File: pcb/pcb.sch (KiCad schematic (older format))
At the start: 19 parts, among them J1 USB_C_Receptacle_USB2.0, SW1 SW_Push, U1 ATmega32U4-AU, U2 PRTR5V0U2X, Y1 16MHz

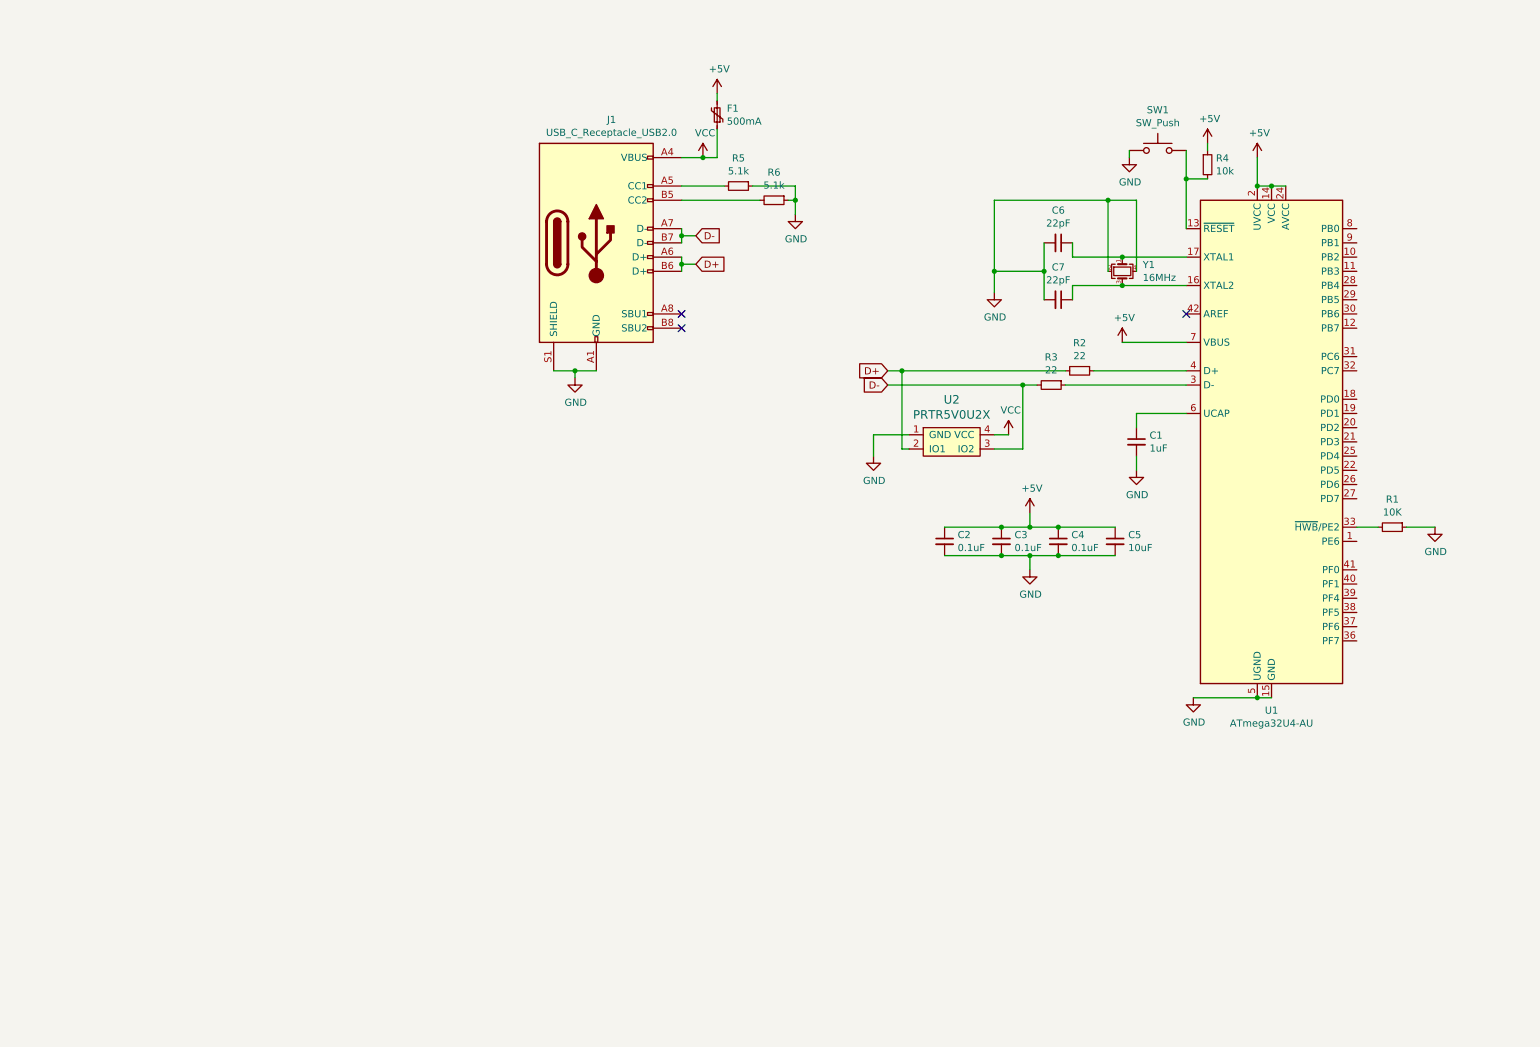
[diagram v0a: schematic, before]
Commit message: set up switch matrix
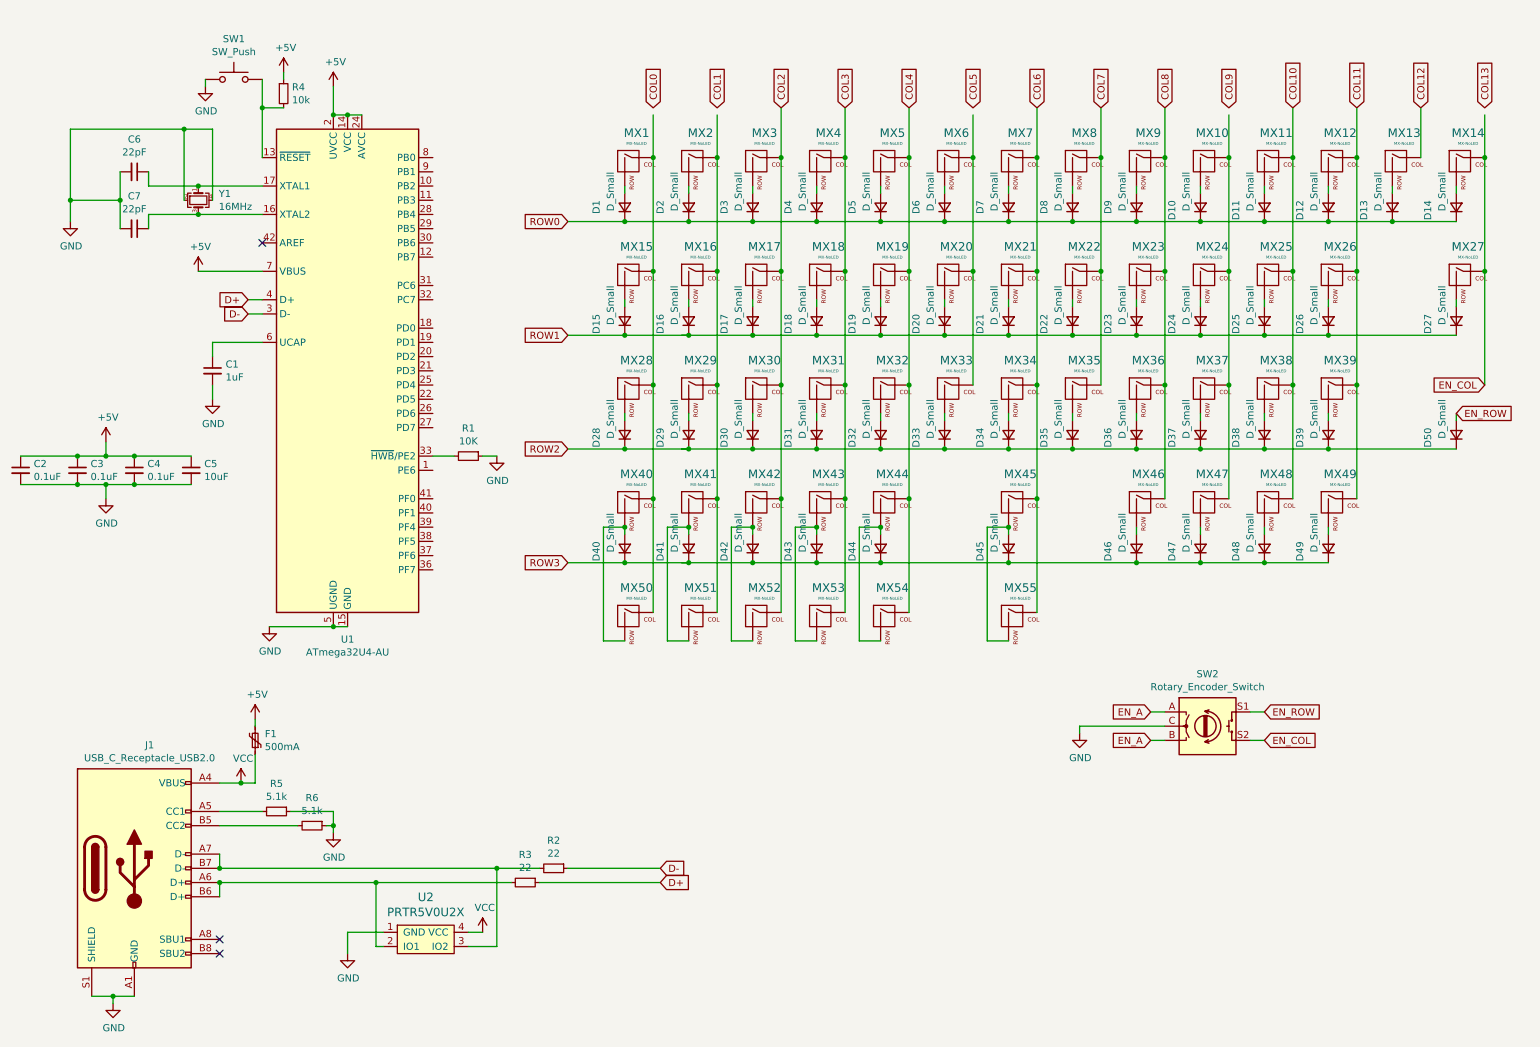
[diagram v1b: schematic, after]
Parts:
- added D1, D10, D11, D12, D13, D14, D15, D16, D17, D18, D19, D2, D20, D21, D22, D23, D24, D25, D26, D27, D28, D29, D3, D30, D31, D32, D33, D34, D35, D36, D37, D38, D39, D4, D40, D41, D42, D43, D44, D45, D46, D47, D48, D49, D5, D50, D6, D7, D8, D9: D_Small, symbol Device:D_Small
- added MX1, MX10, MX11, MX12, MX13, MX14, MX15, MX16, MX17, MX18, MX19, MX2, MX20, MX21, MX22, MX23, MX24, MX25, MX26, MX27, MX28, MX29, MX3, MX30, MX31, MX32, MX33, MX34, MX35, MX36, MX37, MX38, MX39, MX4, MX40, MX41, MX42, MX43, MX44, MX45, MX46, MX47, MX48, MX49, MX5, MX50, MX51, MX52, MX53, MX54, MX55, MX6, MX7, MX8, MX9: MX-NoLED, symbol MX_Alps_Hybrid:MX-NoLED
- added SW2: Rotary_Encoder_Switch, symbol Device:Rotary_Encoder_Switch
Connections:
- net labels added: COL0, COL1, COL10, COL11, COL12, COL13, COL2, COL3, COL4, COL5, COL6, COL7, COL8, COL9, EN_A, EN_COL, EN_ROW, ROW0, ROW1, ROW2, ROW3
- wire segments 73 -> 254
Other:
- moved on the sheet: C1, C2, C3, C4, C5, C6, C7, F1, J1, R1, R2, R3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

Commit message: assign footprints
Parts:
- removed U2: PRTR5V0U2X, symbol random-keyboard-parts:PRTR5V0U2X
- added J2: AVR-ISP-6, symbol Connector:AVR-ISP-6
- added MX56: MX-NoLED, MX_Alps_Hybrid:MX-2U, symbol MX_Alps_Hybrid:MX-NoLED
- C1, C2, C3, C4, C5, C6, C7: footprint (none) -> Capacitor_SMD:C_0805_2012Metric
- D1, D10, D11, D12, D13, D14, D15, D16, D17, D18, D19, D2, D20, D21, D22, D23, D24, D25, D26, D27, D28, D29, D3, D30, D31, D32, D33, D34, D35, D36, D37, D38, D39, D4, D40, D41, D42, D43, D44, D45, D46, D47, D48, D49, D5, D50, D6, D7, D8, D9: footprint (none) -> Diode_SMD:D_SOD-123
- E1: renamed from SW2; footprint (none) -> Rotary_Encoder:RotaryEncoder_Alps_EC11E_Vertical_H20mm
- F1: footprint (none) -> Fuse:Fuse_1206_3216Metric
- J1: footprint (none) -> Connector_USB:USB_C_Receptacle_Palconn_UTC16-G
- MX1, MX10, MX11, MX12, MX13, MX14, MX16, MX17, MX18, MX19, MX2, MX20, MX21, MX22, MX23, MX24, MX25, MX27, MX29, MX3, MX30, MX31, MX32, MX33, MX34, MX35, MX36, MX37, MX38, MX4, MX40, MX41, MX42, MX43, MX46, MX47, MX48, MX49, MX5, MX6, MX7, MX8, MX9: footprint (none) -> MX_Alps_Hybrid:MX-1U
- MX15, MX26: footprint (none) -> MX_Alps_Hybrid:MX-1.5U
- MX28: footprint (none) -> MX_Alps_Hybrid:MX-1.75U
- MX39, MX50, MX51, MX52, MX53, MX55: footprint (none) -> MX_Alps_Hybrid:MX-1.25U
- MX44, MX54: footprint (none) -> MX_Alps_Hybrid:MX-2.75U
- MX45: footprint (none) -> MX_Alps_Hybrid:MX-2.25U
- R1, R2, R3, R4, R5, R6: footprint (none) -> Resistor_SMD:R_0805_2012Metric
- SW1: footprint (none) -> Button_Switch_SMD:SW_SPST_EVQP7C
- Y1: footprint (none) -> Crystal:Crystal_SMD_3225-4Pin_3.2x2.5mm
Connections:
- net labels added: E_A, E_B, E_COL, E_ROW, MISO, MOSI, RST, SCK
- net labels removed: EN_A, EN_COL, EN_ROW
- wire segments 254 -> 257
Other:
- moved on the sheet: D1, D10, D11, D12, D13, D14, D15, D16, D17, D18, D19, D2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

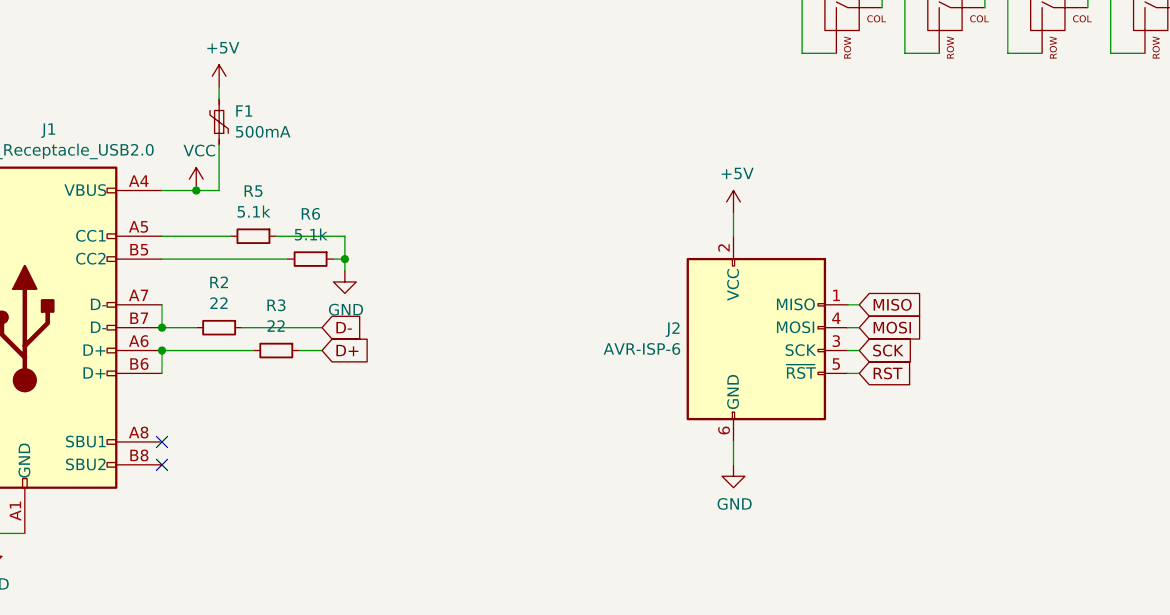
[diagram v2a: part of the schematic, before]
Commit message: add isp footprints
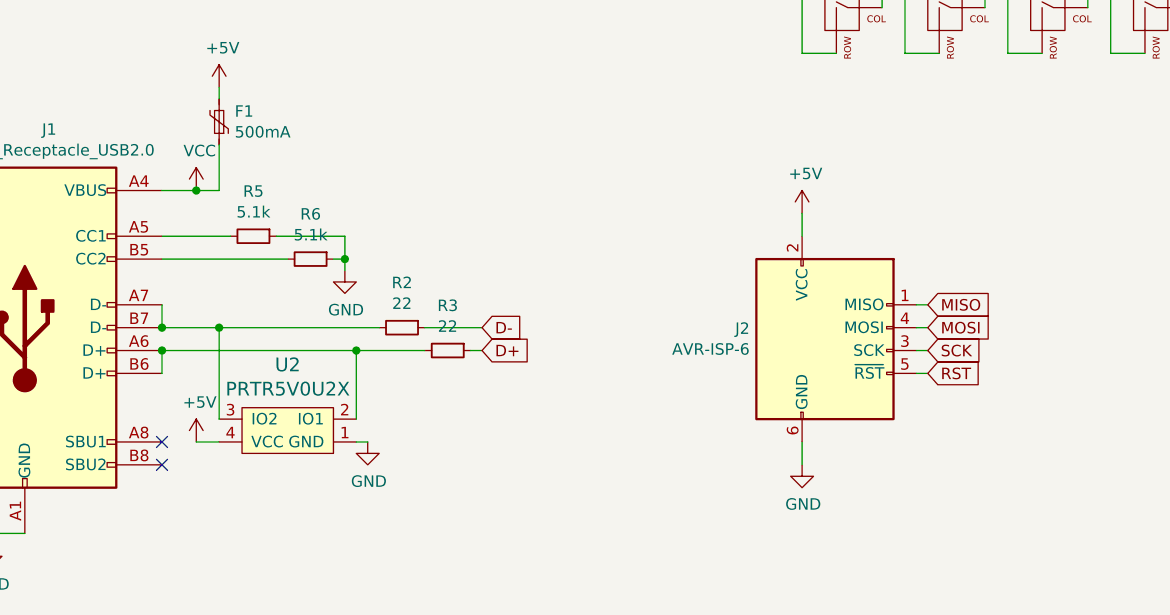
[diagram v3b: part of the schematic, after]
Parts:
- added U2: PRTR5V0U2X, random-keyboard-parts:SOT143B, symbol random-keyboard-parts:PRTR5V0U2X
- J2: footprint (none) -> random-keyboard-parts:Reset_Pretty
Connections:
- wire segments 257 -> 263
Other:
- moved on the sheet: J2, R2, R3
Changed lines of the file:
@@
 Wire Wire Line
 	2050 6400 2050 6500
-Text GLabel 2750 6600 2    50   Input ~ 0
-D+
 $Comp
 L Device:R_Small R2
 U 1 1 61ACD13B
-P 2300 6500
-F 0 "R2" V 2104 6500 50  0000 C CNN
-F 1 "22" V 2195 6500 50  0000 C CNN
-F 2 "Resistor_SMD:R_0805_2012Metric" H 2300 6500 50  0001 C CNN
-F 3 "~" H 2300 6500 50  0001 C CNN
-	1    2300 6500
+P 3100 6500
+F 0 "R2" V 2904 6500 50  0000 C CNN
+F 1 "22" V 2995 6500 50  0000 C CNN
+F 2 "Resistor_SMD:R_0805_2012Metric" H 3100 6500 50  0001 C CNN
+F 3 "~" H 3100 6500 50  0001 C CNN
+	1    3100 6500
 	0    1    1    0
 $EndComp
@@
 L Device:R_Small R3
 U 1 1 61ACDED4
-P 2550 6600
-F 0 "R3" V 2354 6600 50  0000 C CNN
-F 1 "22" V 2445 6600 50  0000 C CNN
-F 2 "Resistor_SMD:R_0805_2012Metric" H 2550 6600 50  0001 C CNN
-F 3 "~" H 2550 6600 50  0001 C CNN
-	1    2550 6600
+P 3300 6600
+F 0 "R3" V 3104 6600 50  0000 C CNN
+F 1 "22" V 3195 6600 50  0000 C CNN
+F 2 "Resistor_SMD:R_0805_2012Metric" H 3300 6600 50  0001 C CNN
+F 3 "~" H 3300 6600 50  0001 C CNN
+	1    3300 6600
 	0    1    1    0
 $EndComp
-Text GLabel 2750 6500 2    50   Input ~ 0
-D-
 Wire Wire Line
 	2300 5450 2300 5500
@@
 	10150 1050 10150 1350
 Connection ~ 10150 1350
-Wire Wire Line
-	2200 6500 2050 6500
 Connection ~ 2050 6500
-Wire Wire Line
-	2050 6600 2450 6600
 Connection ~ 2050 6600
 $Comp
 L power:+5V #PWR0111
 U 1 1 61D89112
-P 4550 6000
-F 0 "#PWR0111" H 4550 5850 50  0001 C CNN
-F 1 "+5V" H 4565 6173 50  0000 C CNN
-F 2 "" H 4550 6000 50  0001 C CNN
-F 3 "" H 4550 6000 50  0001 C CNN
-	1    4550 6000
-	1    0    0    -1
-$EndComp
-Wire Wire Line
-	4550 6000 4550 6100
+P 4850 6000
+F 0 "#PWR0111" H 4850 5850 50  0001 C CNN
+F 1 "+5V" H 4865 6173 50  0000 C CNN
+F 2 "" H 4850 6000 50  0001 C CNN
+F 3 "" H 4850 6000 50  0001 C CNN
+	1    4850 6000
+	1    0    0    -1
+$EndComp
+Wire Wire Line
+	4850 6000 4850 6100
 $Comp
 L power:GND #PWR0112
 U 1 1 61D9AA06
-P 4550 7100
-F 0 "#PWR0112" H 4550 6850 50  0001 C CNN
-F 1 "GND" H 4555 6927 50  0000 C CNN
-F 2 "" H 4550 7100 50  0001 C CNN
-F 3 "" H 4550 7100 50  0001 C CNN
-	1    4550 7100
-	1    0    0    -1
-$EndComp
-Wire Wire Line
-	4550 7000 4550 7100
-Text GLabel 5100 6400 2    50   Input ~ 0
+P 4850 7100
+F 0 "#PWR0112" H 4850 6850 50  0001 C CNN
+F 1 "GND" H 4855 6927 50  0000 C CNN
+F 2 "" H 4850 7100 50  0001 C CNN
+F 3 "" H 4850 7100 50  0001 C CNN
+	1    4850 7100
+	1    0    0    -1
+$EndComp
+Wire Wire Line
+	4850 7000 4850 7100
+Text GLabel 5400 6400 2    50   Input ~ 0
 MISO
-Text GLabel 5100 6500 2    50   Input ~ 0
+Text GLabel 5400 6500 2    50   Input ~ 0
 MOSI
-Text GLabel 5100 6600 2    50   Input ~ 0
+Text GLabel 5400 6600 2    50   Input ~ 0
 SCK
-Text GLabel 5100 6700 2    50   Input ~ 0
+Text GLabel 5400 6700 2    50   Input ~ 0
 RST
 Wire Wire Line
-	5100 6400 5050 6400
-Wire Wire Line
-	5050 6500 5100 6500
+	5400 6400 5350 6400
+Wire Wire Line
+	5350 6500 5400 6500
 $Comp
 L Connector:AVR-ISP-6 J2
 U 1 1 61D861F9
-P 4650 6600
-F 0 "J2" H 4321 6696 50  0000 R CNN
-F 1 "AVR-ISP-6" H 4321 6605 50  0000 R CNN
-F 2 "" V 4400 6650 50  0001 C CNN
-F 3 " ~" H 3375 6050 50  0001 C CNN
-	1    4650 6600
-	1    0    0    -1
-$EndComp
-Wire Wire Line
-	5050 6600 5100 6600
-Wire Wire Line
-	5050 6700 5100 6700
+P 4950 6600
+F 0 "J2" H 4621 6696 50  0000 R CNN
+F 1 "AVR-ISP-6" H 4621 6605 50  0000 R CNN
+F 2 "random-keyboard-parts:Reset_Pretty" V 4700 6650 50  0001 C CNN
+F 3 " ~" H 3675 6050 50  0001 C CNN
+	1    4950 6600
+	1    0    0    -1
+$EndComp
+Wire Wire Line
+	5350 6600 5400 6600
+Wire Wire Line
+	5350 6700 5400 6700
 $Comp
 L power:+5V #PWR0101
@@
 Wire Wire Line
 	9450 5750 9550 5750
-Wire Wire Line
-	2750 6500 2400 6500
-Wire Wire Line
-	2750 6600 2650 6600
+Text GLabel 3450 6500 2    50   Input ~ 0
+D-
+Text GLabel 3450 6600 2    50   Input ~ 0
+D+
+$Comp
+L random-keyboard-parts:PRTR5V0U2X U2
+U 1 1 61B80268
+P 2600 6950
+F 0 "U2" H 2600 6663 60  0000 C CNN
+F 1 "PRTR5V0U2X" H 2600 6769 60  0000 C CNN
+F 2 "random-keyboard-parts:SOT143B" H 2600 6950 60  0001 C CNN
+F 3 "" H 2600 6950 60  0001 C CNN
+	1    2600 6950
+	-1   0    0    1
+$EndComp
+Wire Wire Line
+	3400 6600 3450 6600
+Wire Wire Line
+	3200 6500 3450 6500
+Wire Wire Line
+	2050 6500 2300 6500
+Wire Wire Line
+	2050 6600 2900 6600
+$Comp
+L power:GND #PWR0118
+U 1 1 61C28FEC
+P 2950 7000
+F 0 "#PWR0118" H 2950 6750 50  0001 C CNN
+F 1 "GND" H 2955 6827 50  0000 C CNN
+F 2 "" H 2950 7000 50  0001 C CNN
+F 3 "" H 2950 7000 50  0001 C CNN
+	1    2950 7000
+	1    0    0    -1
+$EndComp
+$Comp
+L power:+5V #PWR0119
+U 1 1 61C3AE4E
+P 2200 7000
+F 0 "#PWR0119" H 2200 6850 50  0001 C CNN
+F 1 "+5V" H 2215 7173 50  0000 C CNN
+F 2 "" H 2200 7000 50  0001 C CNN
+F 3 "" H 2200 7000 50  0001 C CNN
+	1    2200 7000
+	1    0    0    -1
+$EndComp
+Wire Wire Line
+	2300 7000 2200 7000
+Wire Wire Line
+	2900 7000 2950 7000
+Wire Wire Line
+	2300 6900 2300 6500
+Connection ~ 2300 6500
+Wire Wire Line
+	2300 6500 3000 6500
+Wire Wire Line
+	2900 6900 2900 6600
+Connection ~ 2900 6600
+Wire Wire Line
+	2900 6600 3200 6600
 $EndSCHEMATC

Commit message: iso mask footprint
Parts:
- J2: footprint random-keyboard-parts:Reset_Pretty -> random-keyboard-parts:Reset_Pretty-Mask
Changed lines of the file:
@@
 F 0 "J2" H 4621 6696 50  0000 R CNN
 F 1 "AVR-ISP-6" H 4621 6605 50  0000 R CNN
-F 2 "random-keyboard-parts:Reset_Pretty" V 4700 6650 50  0001 C CNN
+F 2 "random-keyboard-parts:Reset_Pretty-Mask" V 4700 6650 50  0001 C CNN
 F 3 " ~" H 3675 6050 50  0001 C CNN
 	1    4950 6600
